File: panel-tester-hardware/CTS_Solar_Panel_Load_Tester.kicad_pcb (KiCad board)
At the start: 2 copper layers, 9 parts, among them J1 Screw_Terminal_01x02, J2 Conn_01x02_Pin, U1 INA219AxD

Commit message: PCB layout v1
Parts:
- added G***: LOGO, LOGO, B.Cu at (83.8, 36.2)
- added J3: Conn_01x07, Connector_PinHeader_2.54mm:PinHeader_1x07_P2.54mm_Vertical, F.Cu at (80.0, 49.1)
- RV1: footprint Potentiometer_Custom:POT_P120PK-x25_TTE -> Potentiometer_Custom:3310C101102L
- moved J1 50.9 mm to (117.5, 57.3), turned to 90 degrees
- moved R1 45.9 mm to (118.8, 40.3), turned to 90 degrees
- moved R_SHUNT3 43.1 mm to (92.5, 58.2), turned to 90 degrees
- moved R2 42.5 mm to (113.0, 40.3), turned to 90 degrees
- moved R3 36.4 mm to (101.0, 48.8), turned to 90 degrees
- moved U1 33.3 mm to (105.5, 39.0), turned to 90 degrees
- moved J2 33.0 mm to (117.0, 65.2)
- moved R4 30.3 mm to (108.2, 48.7), turned to 90 degrees
- moved RV1 28.4 mm to (101.2, 55.9)
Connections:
- net +3.3V renamed +3V3
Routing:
- net V_SOLAR_INPUT_POS: track 0.00 -> 75.6 mm, vias 0 -> 3
- net MCU_ADC_SENSE: track 0.00 -> 50.2 mm, vias 0 -> 2
- net MCU_I2C_SCL: track 0.00 -> 40.4 mm, vias 0 -> 1
- net Net-(U1-IN-): track 0.00 -> 35.9 mm, vias 0 -> 2
- net MCU_I2C_SDA: track 0.00 -> 34.1 mm
- net GND: track 0.00 -> 7.03 mm, vias 0 -> 3
- added copper zone on F.Cu, net +3V3
- added copper zone on B.Cu, net GND
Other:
- board outline added: 50 x 42.5 mm
- board text added: "2025-02-25 Rev. 3"
- board text added: "3v3"
- board text added: "5V"
- board text added: "ADC"
- board text added: "GND"
- board text added: "SCL"
- board text added: "SDA"
- board text added: "VDD"

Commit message: Bluepill layout edits
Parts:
- added U2: YAAJ_BluePill, BluePill:YAAJ_BluePill_2, F.Cu at (97.1, 80.1)
- moved J1 58.7 mm to (144.2, 109.6)
- moved J2 58.7 mm to (143.8, 117.5)
- moved RV1 58.1 mm to (123.7, 109.5)
- moved R_SHUNT3 56.6 mm to (111.0, 111.8)
- moved R1 56.1 mm to (140.3, 92.0)
- moved R2 56.1 mm to (134.6, 92.0)
- moved R3 55.7 mm to (115.8, 102.5)
- moved R4 55.3 mm to (121.0, 102.5)
- moved U1 54.5 mm to (122.8, 90.8)
- moved J3 48.1 mm to (96.8, 94.2)
- moved G*** 31.3 mm to (104.8, 59.5)
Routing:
- net +5V: track 0.00 -> 50.9 mm, vias 0 -> 1
- net MCU_I2C_SDA: track 34.1 -> 50.0 mm, vias 0 -> 2
- net Net-(U1-IN-): track 35.9 -> 51.1 mm
- net MCU_I2C_SCL: track 40.4 -> 53.5 mm, vias 1 -> 0
- net V_SOLAR_INPUT_POS: track 75.6 -> 86.7 mm, vias 3 -> 4
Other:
- board size 50 x 42.5 mm -> 60.1 x 70.5 mm

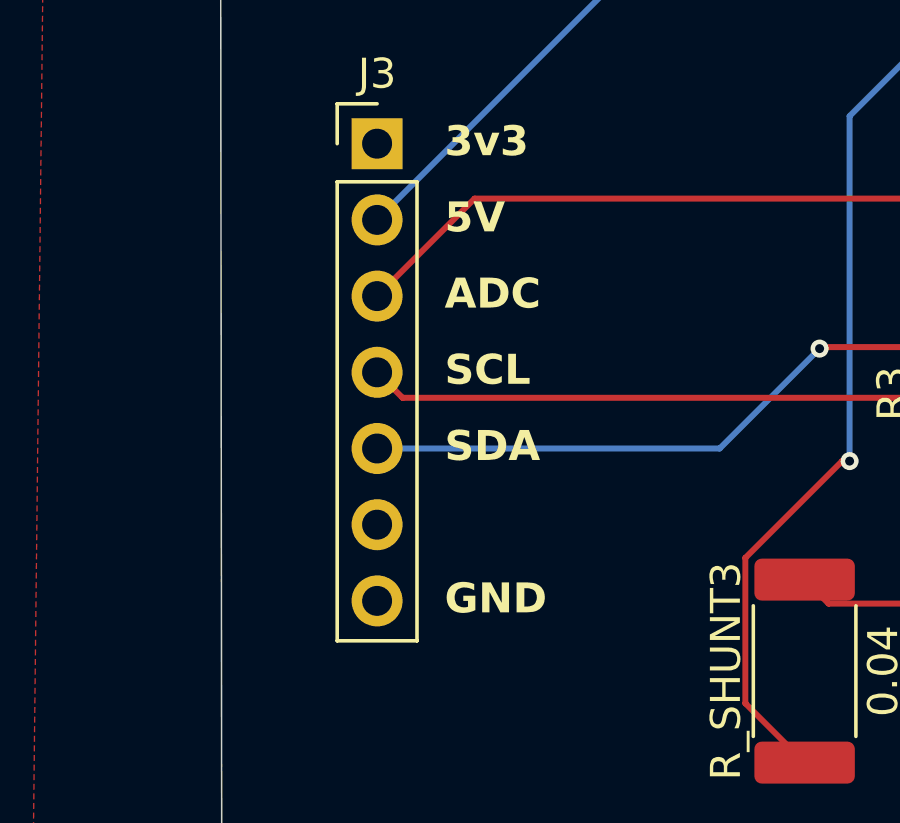
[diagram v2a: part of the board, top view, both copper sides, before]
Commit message: ERC/DRC fixes
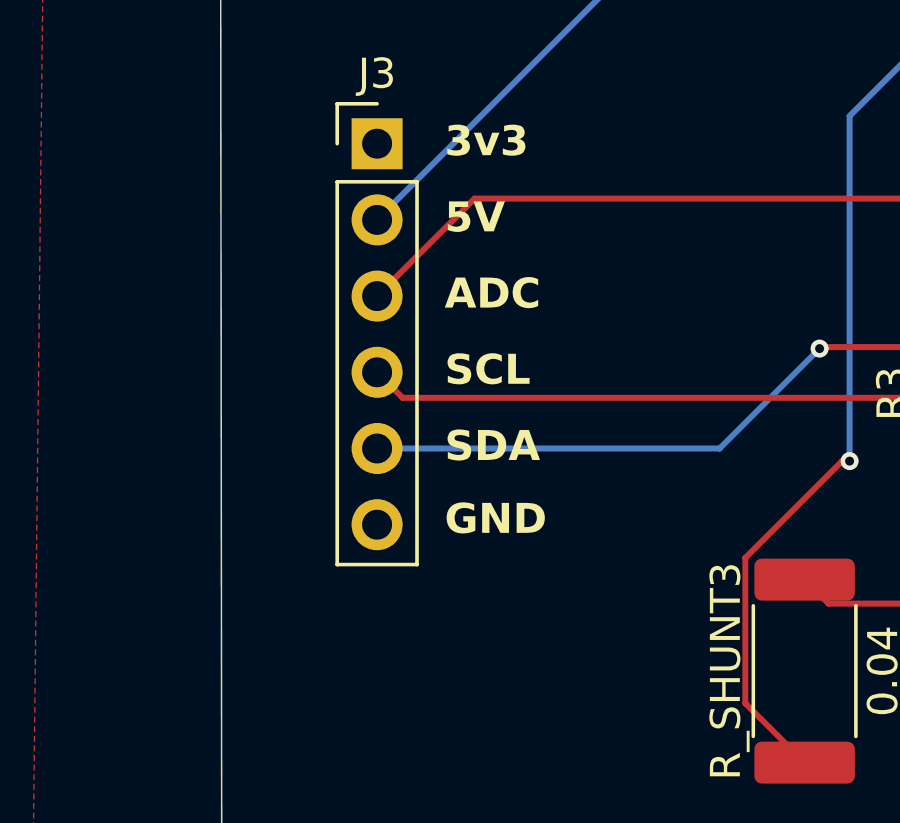
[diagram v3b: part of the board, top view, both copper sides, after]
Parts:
- J3: footprint Connector_PinHeader_2.54mm:PinHeader_1x07_P2.54mm_Vertical -> Connector_PinHeader_2.54mm:PinHeader_1x06_P2.54mm_Vertical
- RV1: footprint Potentiometer_Custom:3310C101102L -> PotentiometerCustom:3310C101102L
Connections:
- J3 pad 6: unconnected-(J3-Pin_6-Pad6) -> GND

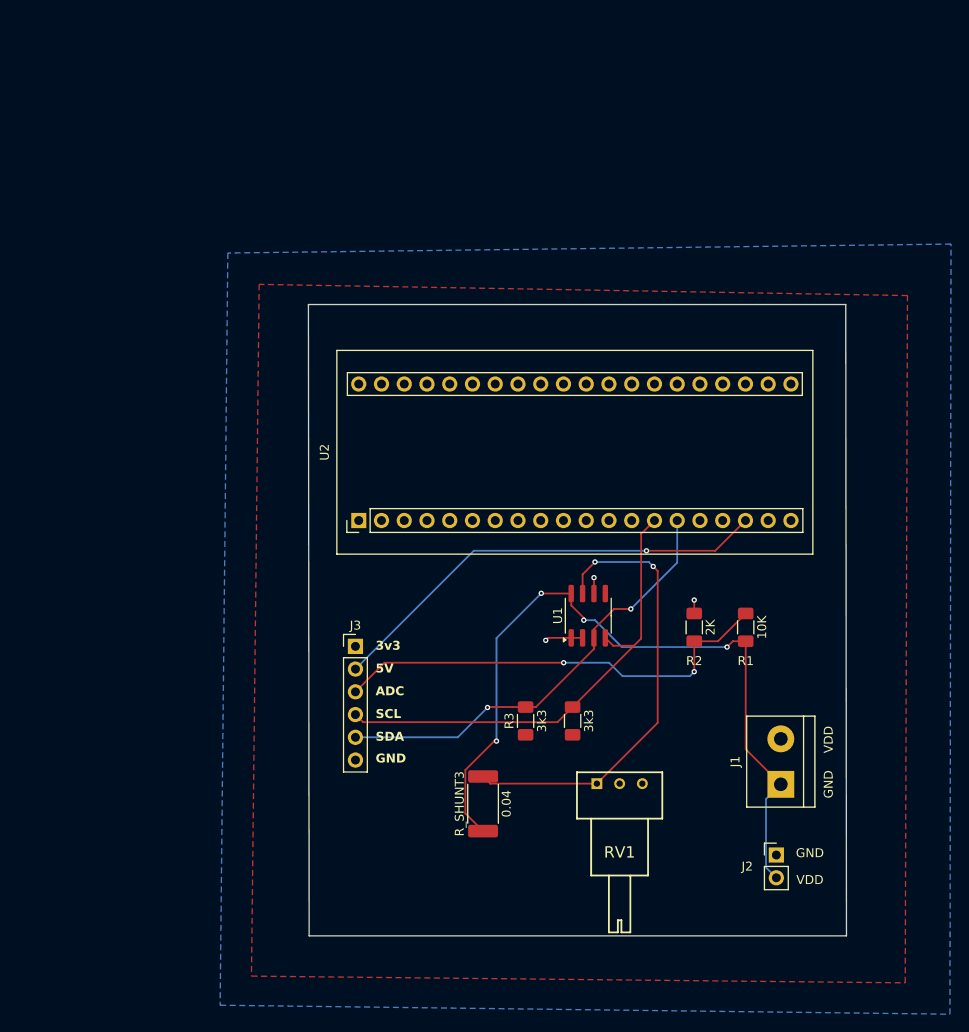
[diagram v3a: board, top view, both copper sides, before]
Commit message: Layout fixes, add mounting holes, silkscreen edits
TODO: Add bypass capacitor & reroute, use thicker trace for high current path
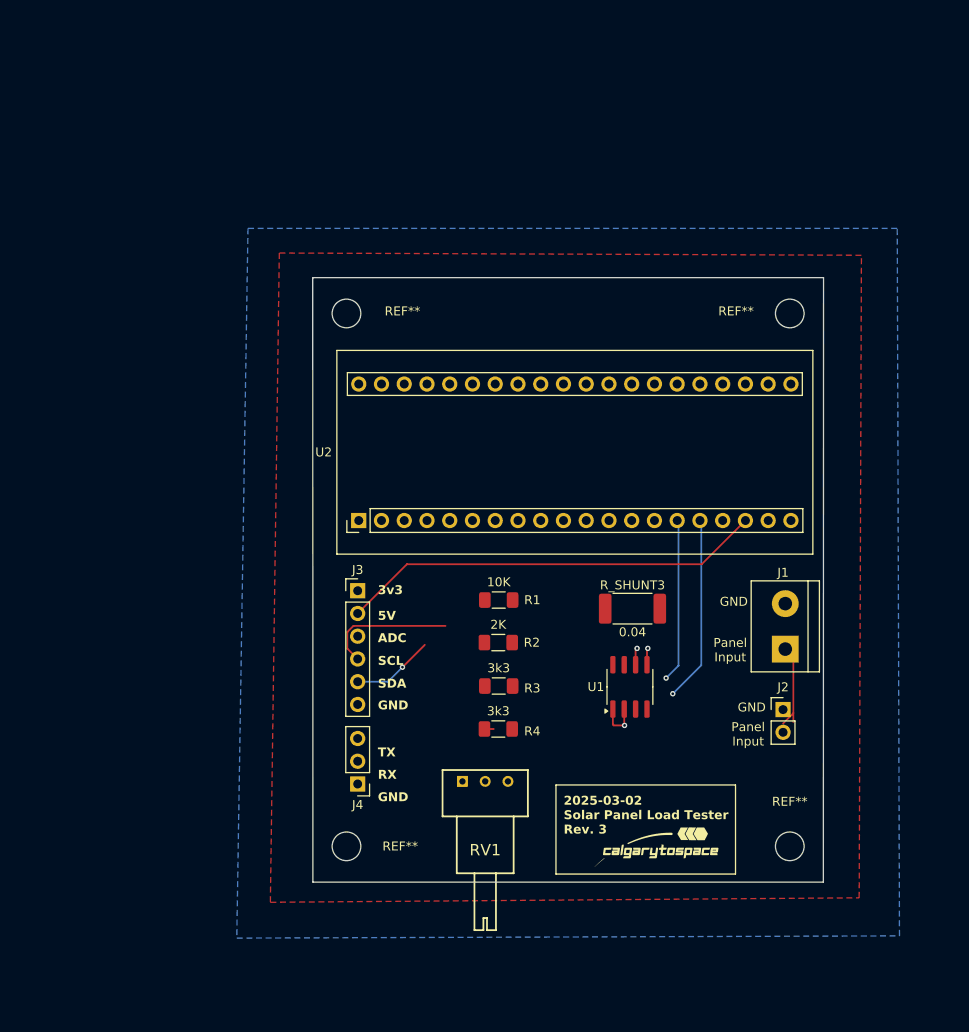
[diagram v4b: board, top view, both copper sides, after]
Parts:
- added J4: Conn_01x03, Connector_PinHeader_2.54mm:PinHeader_1x03_P2.54mm_Vertical, F.Cu at (97.0, 109.5)
- added REF**: MountingHole_3.2mm_M3, MountingHole:MountingHole_3.2mm_M3, F.Cu at (145.2, 116.5)
- added REF**: MountingHole_3.2mm_M3, MountingHole:MountingHole_3.2mm_M3, F.Cu at (145.2, 57.0)
- added REF**: MountingHole_3.2mm_M3, MountingHole:MountingHole_3.2mm_M3, F.Cu at (95.8, 116.5)
- added REF**: MountingHole_3.2mm_M3, MountingHole:MountingHole_3.2mm_M3, F.Cu at (95.8, 57.0)
- G***: moved to F.Cu
- moved G*** 62.4 mm to (130.2, 116.5), turned to 0 degrees
- moved R1 27.7 mm to (112.8, 89.0), turned to 180 degrees
- moved R_SHUNT3 27.4 mm to (127.7, 90.0), turned to 0 degrees
- moved R2 21.9 mm to (112.7, 93.8), turned to 180 degrees
- moved J2 16.3 mm to (144.5, 101.2)
- moved J1 15.1 mm to (144.8, 94.5)
- moved RV1 15.0 mm to (108.7, 109.2)
- moved U1 9.21 mm to (127.4, 98.7)
- moved R4 8.35 mm to (112.7, 103.4), turned to 180 degrees
- moved J3 6.22 mm to (97.0, 88.0)
- moved R3 4.92 mm to (112.8, 98.6), turned to 180 degrees
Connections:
- U2 pad 6: unconnected-(U2-PA9-Pad6) -> Net-(J4-Pin_3)
- U2 pad 7: unconnected-(U2-PA10-Pad7) -> Net-(J4-Pin_2)
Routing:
- net V_SOLAR_INPUT_POS: track 86.7 -> 10.1 mm, vias 4 -> 0
- net Net-(U1-IN-): track 51.1 -> 0.00 mm, vias 2 -> 0
- net MCU_ADC_SENSE: track 50.4 -> 0.00 mm, vias 2 -> 0
- net MCU_I2C_SCL: track 53.5 -> 15.8 mm
- net MCU_I2C_SDA: track 50.0 -> 27.4 mm
- net unconnected-(U2-PB8-Pad16): track 0.00 -> 20.7 mm, vias 0 -> 1
- net +5V: track 50.9 -> 47.6 mm, vias 1 -> 0
- net +3V3: track 0.00 -> 1.86 mm, vias 0 -> 1
- net GND: track 7.50 -> 6.66 mm, vias 3 -> 2
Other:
- board size 60.1 x 70.5 mm -> 57 x 67.5 mm
- board text added: "2025-03-02 Solar Panel Load Tester Rev. 3"
- board text added: "Panel Input"
- board text added: "R4"
- board text added: "RX"
- board text added: "TX"
- board text removed: "2025-02-25 Rev. 3"
- board text removed: "VDD"

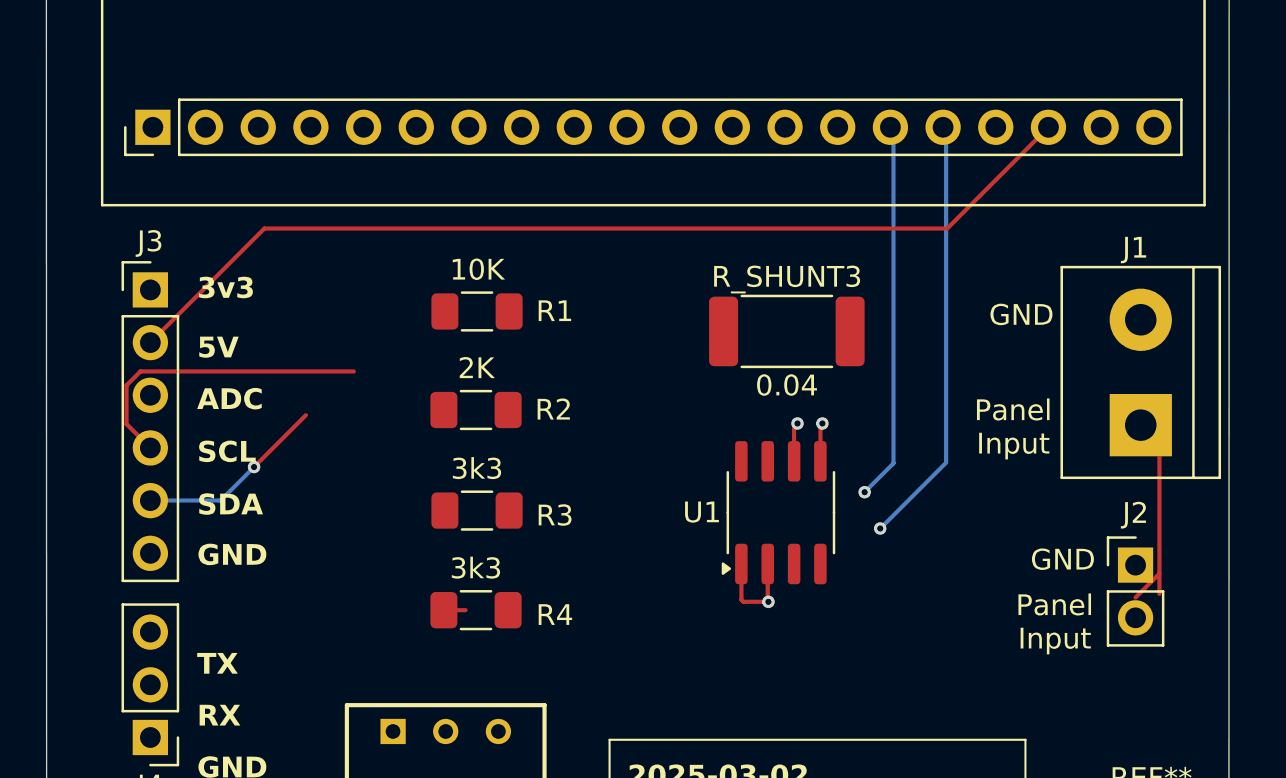
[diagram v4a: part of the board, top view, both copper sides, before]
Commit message: Add bypass capacitor
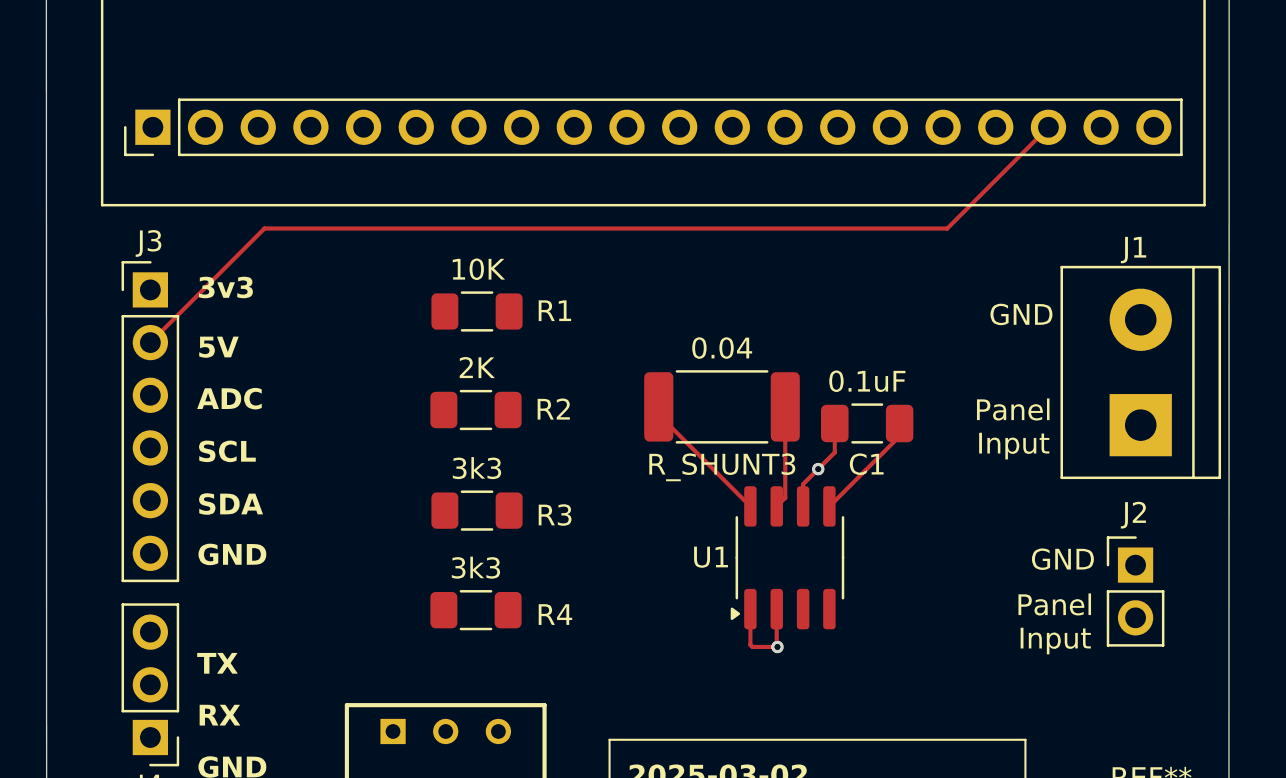
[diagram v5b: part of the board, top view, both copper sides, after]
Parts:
- added C1: 0.1uF, Capacitor_SMD:C_1206_3216Metric_Pad1.33x1.80mm_HandSolder, F.Cu at (131.6, 94.4)
- moved R_SHUNT3 4.80 mm to (124.6, 93.6)
- moved U1 2.22 mm to (127.8, 100.9)
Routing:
- net MCU_I2C_SDA: track 27.4 -> 0.00 mm, vias 2 -> 0
- net unconnected-(U2-PB8-Pad16): track 20.7 -> 0.00 mm, vias 1 -> 0
- net MCU_I2C_SCL: track 15.8 -> 0.00 mm
- net Net-(U1-IN-): track 0.00 -> 4.97 mm
- net +3V3: track 1.86 -> 5.40 mm, vias 1 -> 0
- net V_SOLAR_INPUT_POS: track 10.1 -> 6.63 mm
- net GND: track 6.66 -> 9.40 mm

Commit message: Routing
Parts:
- moved R1 1.31 mm to (111.5, 89.4)
- moved R2 1.31 mm to (111.5, 94.2)
- moved R3 1.31 mm to (111.5, 99.0)
- moved R4 1.31 mm to (111.5, 103.8)
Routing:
- net MCU_I2C_SCL: track 0.00 -> 67.3 mm, vias 0 -> 1
- net MCU_I2C_SDA: track 0.00 -> 63.3 mm, vias 0 -> 2
- net V_SOLAR_INPUT_POS: track 6.63 -> 50.4 mm
- net Net-(U1-IN-): track 4.97 -> 28.8 mm, vias 0 -> 1
- net MCU_ADC_SENSE: track 0.00 -> 20.5 mm
- net GND: track 9.40 -> 11.6 mm, vias 2 -> 3
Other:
- board text added: "Solar Panel Load Tester 2025-03-02 Rev. 3"
- board text removed: "2025-03-02 Solar Panel Load Tester Rev. 3"

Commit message: 1.5 mm net class for solar panel input path
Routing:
- net Net-(J4-Pin_2): track 0.00 -> 38.6 mm
- net Net-(J4-Pin_3): track 0.00 -> 35.2 mm
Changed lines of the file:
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@@
 	)
 	(gr_text "RX"
-		(at 99.25 108.5 0)
+		(at 99.25 107.5 0)
 		(layer "F.SilkS")
 		(effects
@@
 	)
 	(gr_text "GND"
-		(at 99.25 111 0)
+		(at 99.25 110 0)
 		(layer "F.SilkS")
 		(effects
@@
 	)
 	(gr_text "TX"
-		(at 99.25 106 0)
+		(at 99.25 105 0)
 		(layer "F.SilkS")
 		(effects
@@
 	)
 	(segment
+		(start 127.6125 97.9875)
+		(end 127.2 98.4)
+		(width 0.2)
+		(layer "F.Cu")
+		(net 3)
+	)
+	(segment
 		(start 127.2 98.4)
 		(end 127.2 99.8)
-		(width 0.2)
-		(layer "F.Cu")
-		(net 3)
-	)
-	(segment
-		(start 127.6125 97.9875)
-		(end 127.2 98.4)
 		(width 0.2)
 		(layer "F.Cu")
@@
 		(net 9)
 	)
+	(segment
+		(start 106.54 104.46)
+		(end 97 104.46)
+		(width 0.2)
+		(layer "B.Cu")
+		(net 15)
+	)
+	(segment
+		(start 109.82 80.12)
+		(end 109.82 101.18)
+		(width 0.2)
+		(layer "B.Cu")
+		(net 15)
+	)
+	(segment
+		(start 109.82 101.18)
+		(end 106.54 104.46)
+		(width 0.2)
+		(layer "B.Cu")
+		(net 15)
+	)
+	(segment
+		(start 112.36 100.84)
+		(end 106.2 107)
+		(width 0.2)
+		(layer "B.Cu")
+		(net 22)
+	)
+	(segment
+		(start 106.2 107)
+		(end 97 107)
+		(width 0.2)
+		(layer "B.Cu")
+		(net 22)
+	)
+	(segment
+		(start 112.36 80.12)
+		(end 112.36 100.84)
+		(width 0.2)
+		(layer "B.Cu")
+		(net 22)
+	)
 	(zone
